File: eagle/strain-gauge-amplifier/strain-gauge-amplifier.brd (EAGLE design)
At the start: 49.8 x 40.3 mm, 25 parts, among them IC2 INA125U, M1 #4-BARE_MOUNTING_HOLE/.300, M2 #4-BARE_MOUNTING_HOLE/.300, M3 #4-BARE_MOUNTING_HOLE/.300, M4 #4-BARE_MOUNTING_HOLE/.300, Q1 PMV45EN

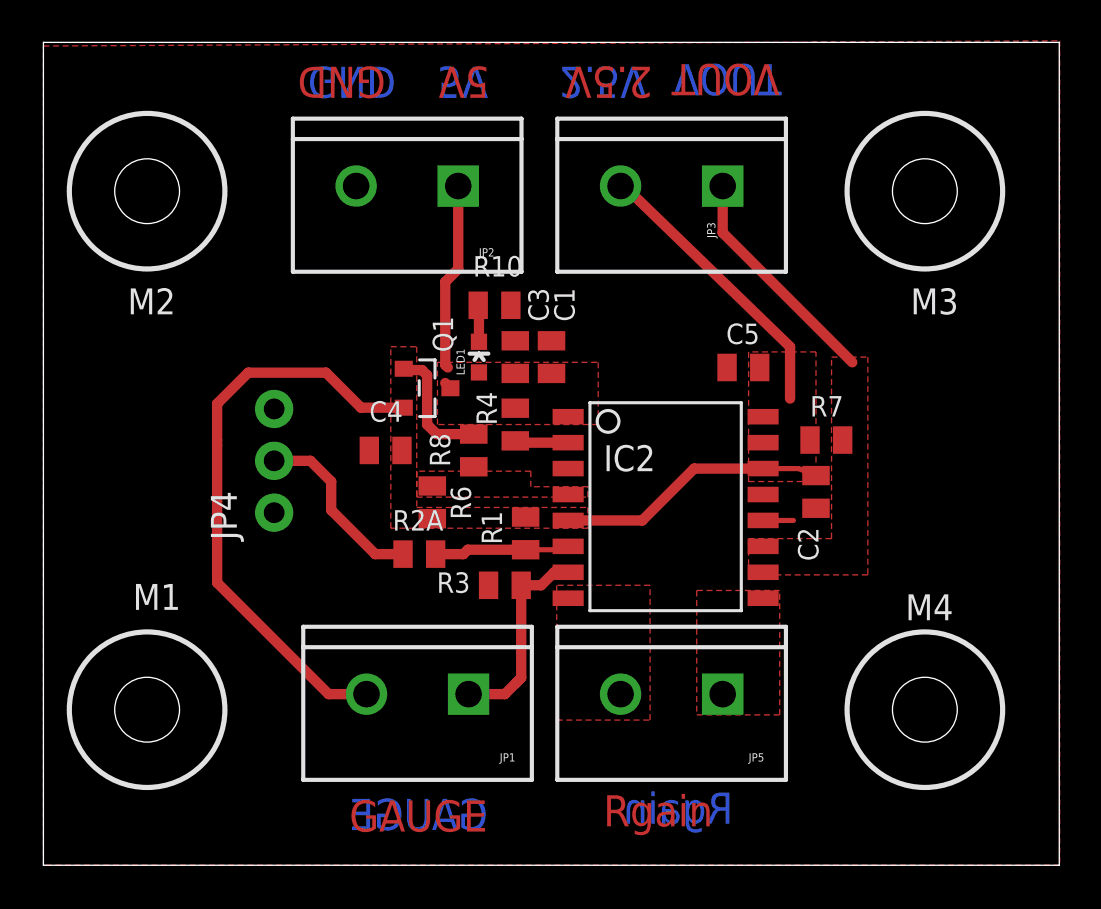
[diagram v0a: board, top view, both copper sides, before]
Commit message: new straingauge board for 4 white strain gauge.
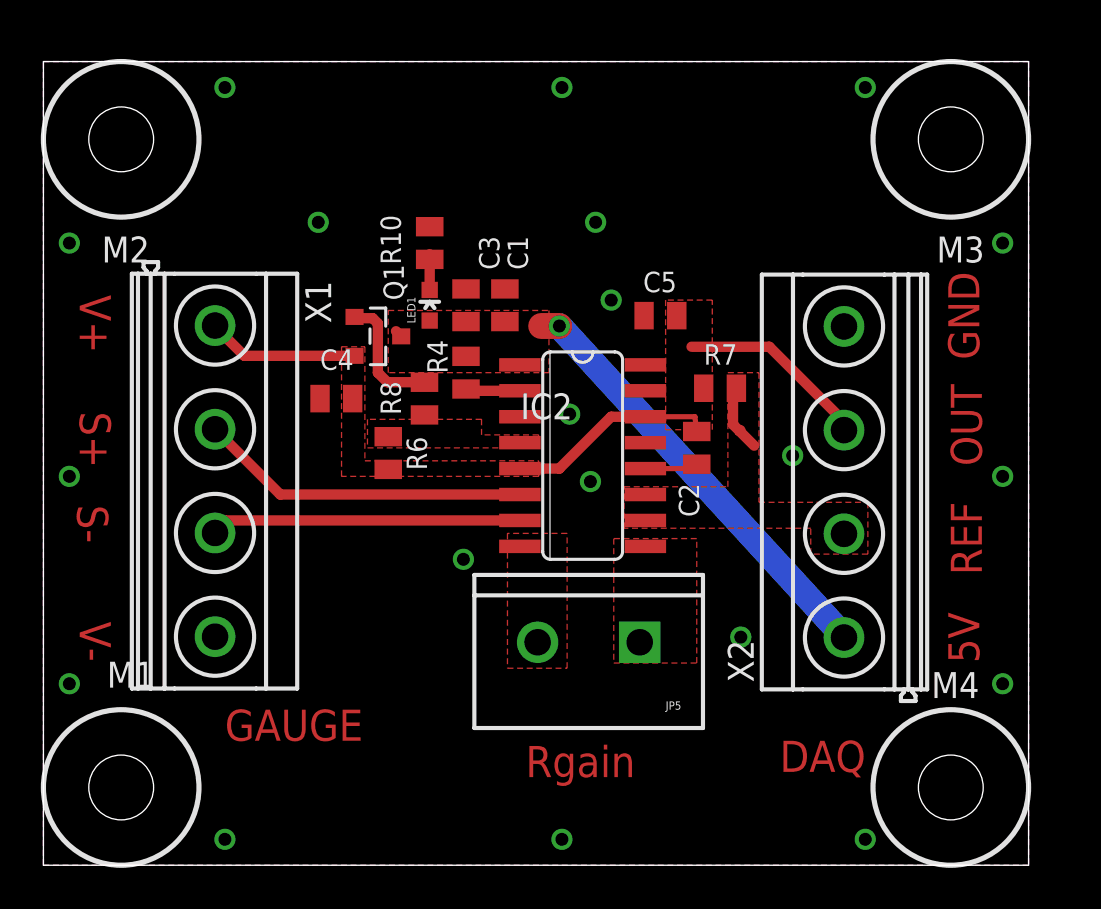
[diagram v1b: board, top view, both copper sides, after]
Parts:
- removed JP1: STRAIN, SparkFun-Connectors:SCREWTERMINAL-5MM-2
- removed JP2, JP3: (no value), SparkFun-Connectors:SCREWTERMINAL-5MM-2
- removed JP4: 10ohm/20turn, SparkFun-Connectors:1X03_NO_SILK
- removed R1, R3: 120 1%, rcl_custom:0805-C-NOSILK
- removed R2A: 115 1%, rcl_custom:0805-C-NOSILK
- added X1, X2: MKDSN1,5/4-5,08, con-phoenix-508:MKDSN1,5/4-5,08
- IC2: value INA125U -> INA125; device burr-brown:SO16-1 -> burr-brown:SO16
- moved C2 6.23 mm to (32.0, 20.4)
- moved R7 5.79 mm to (33.1, 23.4)
- moved JP5 4.79 mm to (29.2, 10.9)
- moved C5 4.79 mm to (30.2, 26.9)
- moved IC2 4.79 mm to (26.4, 20.1)
- moved R10 4.40 mm to (18.9, 30.5), turned to 270 degrees
- moved M4 4.02 mm to (44.5, 3.81)
- moved M1 4.02 mm to (3.81, 3.81)
- moved Q1 3.50 mm to (16.4, 25.9)
- moved C3 3.50 mm to (20.7, 27.4)
- moved LED1 3.50 mm to (18.9, 27.4)
- moved R4 3.50 mm to (20.7, 24.1)
- moved R8 3.50 mm to (18.7, 22.9)
- moved C4 3.50 mm to (14.4, 22.9)
- moved C1 3.42 mm to (22.6, 27.4)
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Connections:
- removed net N$1: JP4.2, R2A.1
- removed net VIN-: IC2.7, JP1.1, R3.2
- new net N$2: IC2.7, X1.3
- net 2.5VREF: now also X1.1, X2.3; no longer JP1.2, JP3.2, R1.2
- net 5V: now also X2.1; no longer JP2.1
- net GND: now also X1.4, X2.4; no longer JP2.2, JP4.3, R3.1
- net VIN+: now also X1.2; no longer R1.1, R2A.2
- net VOUT: now also X2.2; no longer JP3.1
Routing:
- net 2.5VREF: track 56.1 -> 27.3 mm
- net N$2: track 0.00 -> 15.2 mm
- net 5V: track 9.56 -> 21.9 mm, vias 0 -> 1
- net VIN-: track 10.0 -> 0.00 mm
- net VIN+: track 6.65 -> 16.3 mm
- net N$1: track 9.02 -> 0.00 mm
- net VOUT: track 11.3 -> 3.44 mm
- net GND: track 1.49 -> 2.73 mm, vias 0 -> 20
- added copper zone on layer 16, net GND
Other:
- board size 49.8 x 40.3 mm -> 48.3 x 39.4 mm
- board text added: "DAQ"
- board text added: "OUT"
- board text added: "REF"
- board text added: "S+"
- board text added: "S-"
- board text added: "V+"
- board text added: "V-"
- board text removed: "2.5V"
- board text removed: "VOUT"
